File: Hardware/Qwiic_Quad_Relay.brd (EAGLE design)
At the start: 82.5 x 47 mm, 129 parts, among them J2 Qwiic Right Angle, J3 Qwiic Right Angle, J4 POWER_JACK, J9 AVR_SPI_PROG_3X2TESTPOINTS, K1 RELAY-SPDT-JZC-11F, K2 RELAY-SPDT-JZC-11F, K3 RELAY-SPDT-JZC-11F, K4 RELAY-SPDT-JZC-11F, Q1 600mA/40V, Q2 600mA/40V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

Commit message: Removes Buzzard lables and old production files
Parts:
- moved FRAME1 19.2 mm to (7.62, -12.7)
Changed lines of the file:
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@@
 <setting verticaltext="up"/>
 </settings>
-<grid distance="0.05" unitdist="inch" unit="inch" style="lines" multiple="1" display="yes" altdistance="0.002" altunitdist="inch" altunit="inch"/>
+<grid distance="0.05" unitdist="inch" unit="inch" style="lines" multiple="1" display="yes" altdistance="0.005" altunitdist="inch" altunit="inch"/>
 <layers>
 <layer number="1" name="Top" color="4" fill="1" visible="yes" active="yes"/>
@@
 <layer number="115" name="ReferenceISLANDS" color="7" fill="1" visible="no" active="no"/>
 <layer number="116" name="Patch_BOT" color="9" fill="4" visible="no" active="no"/>
-<layer number="117" name="PM_Ref" color="26" fill="1" visible="no" active="yes"/>
+<layer number="117" name="PM_Ref" color="26" fill="1" visible="yes" active="yes"/>
 <layer number="118" name="Rect_Pads" color="7" fill="1" visible="no" active="no"/>
-<layer number="119" name="PF_Ref" color="31" fill="1" visible="no" active="yes"/>
-<layer number="120" name="WFL_Ref" color="25" fill="1" visible="no" active="yes"/>
+<layer number="119" name="PF_Ref" color="31" fill="1" visible="yes" active="yes"/>
+<layer number="120" name="WFL_Ref" color="25" fill="1" visible="yes" active="yes"/>
 <layer number="121" name="_tsilk" color="7" fill="1" visible="no" active="no"/>
 <layer number="122" name="_bsilk" color="7" fill="1" visible="no" active="no"/>
@@
 <wire x1="82.55" y1="2.54" x2="82.55" y2="44.45" width="0.2032" layer="20"/>
 <wire x1="82.55" y1="44.45" x2="80.01" y2="46.99" width="0.2032" layer="20" curve="90"/>
-<text x="40.513" y="-16.637" size="1.778" layer="51" font="vector">Elias Santistevan</text>
+<text x="39.243" y="-12.827" size="1.778" layer="51" font="vector">Elias Santistevan</text>
 <text x="81.534" y="12.319" size="1.778" layer="16" font="vector" ratio="15" rot="SMR270">v20</text>
 <text x="24.892" y="19.812" size="0.381" layer="20" font="vector" rot="R90">Route Out</text>
@@
 <attribute name="VALUE" x="56.9722" y="37.7698" size="0.6096" layer="27" font="vector" ratio="20" align="bottom-center"/>
 </element>
-<element name="FRAME1" library="SparkFun-Aesthetics" package="CREATIVE_COMMONS" value="FRAME-LEDGER" x="10.16" y="-31.75" smashed="yes">
-<attribute name="DESIGNER" value="" x="10.16" y="-31.75" size="1.778" layer="27" display="off"/>
-<attribute name="REV" value="" x="10.16" y="-31.75" size="1.778" layer="27" display="off"/>
+<element name="FRAME1" library="SparkFun-Aesthetics" package="CREATIVE_COMMONS" value="FRAME-LEDGER" x="7.62" y="-12.7" smashed="yes">
+<attribute name="DESIGNER" value="" x="7.62" y="-12.7" size="1.778" layer="27" display="off"/>
+<attribute name="REV" value="" x="7.62" y="-12.7" size="1.778" layer="27" display="off"/>
 </element>
 <element name="C2" library="SparkFun-Capacitors" package="0402" value="0.1uF" x="54.8132" y="43.1546" smashed="yes" rot="R90">

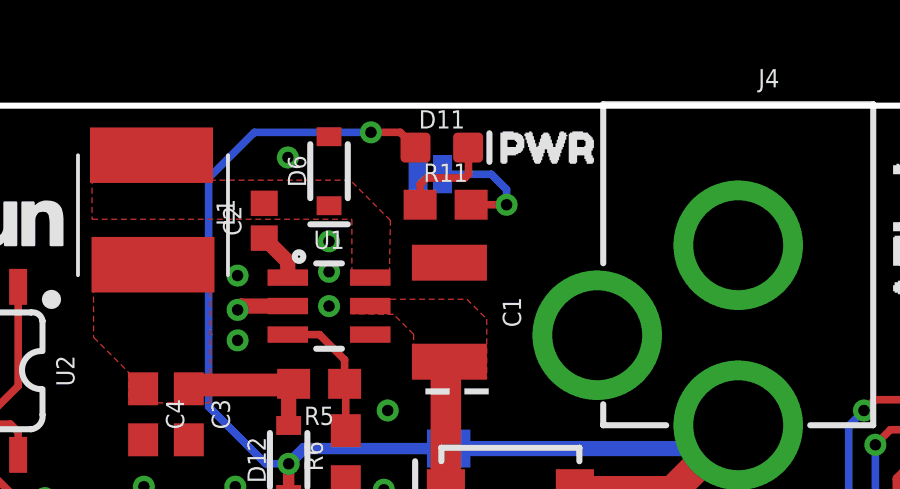
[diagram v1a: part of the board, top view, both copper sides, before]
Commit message: Changes LED jumper to normally closed with trace
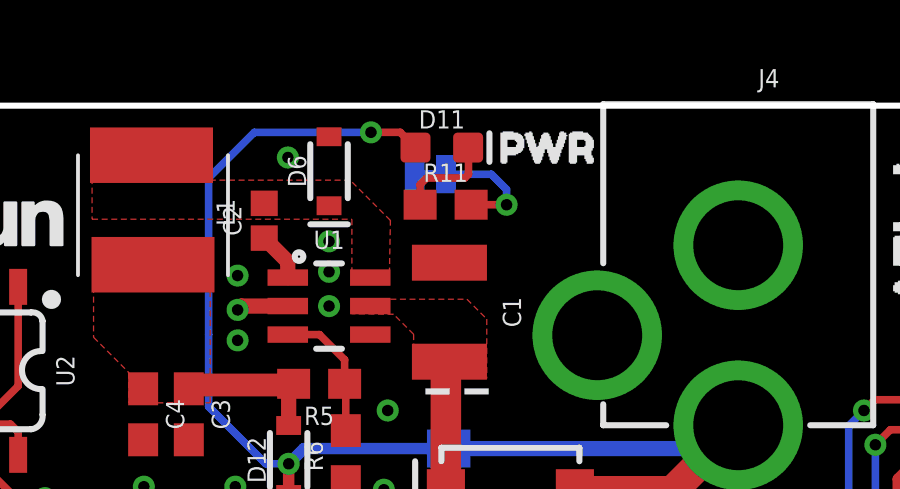
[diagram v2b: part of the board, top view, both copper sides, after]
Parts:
- LED: value JUMPER-SMT_2_NO_SILK -> JUMPER-SMT_2_NC_TRACE_SILK; device SparkFun-Jumpers:SMT-JUMPER_2_NO_SILK -> SparkFun-Jumpers:SMT-JUMPER_2_NC_TRACE_SILK
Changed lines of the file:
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@@
 <?xml version="1.0" encoding="utf-8"?>
 <!DOCTYPE eagle SYSTEM "eagle.dtd">
-<eagle version="9.5.2">
+<eagle version="9.5.1">
 <drawing>
 <settings>
@@
 <attribute name="VALUE" x="57.7342" y="44.8056" size="0.6096" layer="27" font="vector" ratio="20" rot="R90" align="top-center"/>
 </element>
-<element name="LED" library="SparkFun-Jumpers" package="SMT-JUMPER_2_NO_SILK" package3d_urn="urn:adsk.eagle:package:39279/1" value="JUMPER-SMT_2_NO_SILK" x="60.3504" y="44.704" smashed="yes" rot="MR180">
+<element name="LED" library="SparkFun-Jumpers" package="SMT-JUMPER_2_NC_TRACE_SILK" package3d_urn="urn:adsk.eagle:package:39281/1" value="JUMPER-SMT_2_NC_TRACE_SILK" x="60.3504" y="44.704" smashed="yes" rot="MR180">
 <attribute name="NAME" x="60.3504" y="43.561" size="0.6096" layer="26" font="vector" ratio="20" rot="MR180" align="bottom-center"/>
 <attribute name="VALUE" x="60.3504" y="45.847" size="0.6096" layer="28" font="vector" ratio="20" rot="MR180" align="top-center"/>
@@
 <wire x1="62.8904" y1="43.688" x2="62.8904" y2="44.196" width="0.254" layer="16"/>
 <wire x1="62.8904" y1="44.196" x2="62.3824" y2="44.704" width="0.254" layer="16"/>
-<wire x1="62.3824" y1="44.704" x2="60.7568" y2="44.704" width="0.254" layer="16"/>
+<wire x1="62.3824" y1="44.704" x2="60.8711" y2="44.704" width="0.254" layer="16"/>
 </signal>
 <signal name="N$1">

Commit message: Replaces 33 Ohm resistors with 0 Ohm
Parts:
- R10, R2, R4, R8: value 33 -> 0
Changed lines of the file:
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@@
 <attribute name="VALUE" x="20.447" y="19.05" size="0.6096" layer="27" font="vector" ratio="20" rot="R270" align="top-center"/>
 </element>
-<element name="R2" library="SparkFun-Resistors" package="0603" value="33" x="16.637" y="28.1266" smashed="yes" rot="R90">
+<element name="R2" library="SparkFun-Resistors" package="0603" value="0" x="16.637" y="28.1266" smashed="yes" rot="R90">
 <attribute name="NAME" x="15.875" y="28.1266" size="0.6096" layer="25" font="vector" ratio="20" rot="R90" align="bottom-center"/>
-<attribute name="PROD_ID" value="RES-08270" x="16.637" y="28.1266" size="1.778" layer="27" rot="R90" display="off"/>
-<attribute name="VALUE" value="33" x="17.399" y="28.1266" size="0.6096" layer="27" font="vector" ratio="20" rot="R90" align="top-center"/>
+<attribute name="PROD_ID" value="RES-08609" x="16.637" y="28.1266" size="1.778" layer="27" rot="R90" display="off"/>
+<attribute name="VALUE" value="0" x="17.399" y="28.1266" size="0.6096" layer="27" font="vector" ratio="20" rot="R90" align="top-center"/>
 </element>
 <element name="R1" library="SparkFun-Resistors" package="0603" value="1k" x="9.017" y="28.1266" smashed="yes" rot="R90">
@@
 <attribute name="VALUE" x="38.735" y="27.92105" size="0.6096" layer="27" font="vector" ratio="20" rot="R270" align="top-center"/>
 </element>
-<element name="R4" library="SparkFun-Resistors" package="0603" value="33" x="37.211" y="27.9996" smashed="yes" rot="R90">
+<element name="R4" library="SparkFun-Resistors" package="0603" value="0" x="37.211" y="27.9996" smashed="yes" rot="R90">
 <attribute name="NAME" x="36.449" y="27.9996" size="0.6096" layer="25" font="vector" ratio="20" rot="R90" align="bottom-center"/>
-<attribute name="PROD_ID" value="RES-08270" x="37.211" y="27.9996" size="1.778" layer="27" font="vector" ratio="15" rot="R90" display="off"/>
-<attribute name="VALUE" value="33" x="37.973" y="27.9996" size="0.6096" layer="27" font="vector" ratio="20" rot="R90" align="top-center"/>
+<attribute name="PROD_ID" value="RES-08609" x="37.211" y="27.9996" size="1.778" layer="27" font="vector" ratio="15" rot="R90" display="off"/>
+<attribute name="VALUE" value="0" x="37.973" y="27.9996" size="0.6096" layer="27" font="vector" ratio="20" rot="R90" align="top-center"/>
 </element>
-<element name="R8" library="SparkFun-Resistors" package="0603" value="33" x="57.404" y="27.9996" smashed="yes" rot="R90">
+<element name="R8" library="SparkFun-Resistors" package="0603" value="0" x="57.404" y="27.9996" smashed="yes" rot="R90">
 <attribute name="NAME" x="56.642" y="27.9996" size="0.6096" layer="25" font="vector" ratio="20" rot="R90" align="bottom-center"/>
-<attribute name="PROD_ID" value="RES-08270" x="57.404" y="27.9996" size="1.778" layer="27" font="vector" ratio="15" rot="R90" display="off"/>
-<attribute name="VALUE" value="33" x="58.166" y="27.9996" size="0.6096" layer="27" font="vector" ratio="20" rot="R90" align="top-center"/>
+<attribute name="PROD_ID" value="RES-08609" x="57.404" y="27.9996" size="1.778" layer="27" font="vector" ratio="15" rot="R90" display="off"/>
+<attribute name="VALUE" value="0" x="58.166" y="27.9996" size="0.6096" layer="27" font="vector" ratio="20" rot="R90" align="top-center"/>
 </element>
-<element name="R10" library="SparkFun-Resistors" package="0603" value="33" x="77.978" y="27.7837" smashed="yes" rot="R90">
+<element name="R10" library="SparkFun-Resistors" package="0603" value="0" x="77.978" y="27.7837" smashed="yes" rot="R90">
 <attribute name="NAME" x="77.216" y="27.7837" size="0.6096" layer="25" font="vector" ratio="20" rot="R90" align="bottom-center"/>
-<attribute name="PROD_ID" value="RES-08270" x="77.978" y="27.7837" size="1.778" layer="27" font="vector" ratio="15" rot="R90" display="off"/>
-<attribute name="VALUE" value="33" x="78.74" y="27.7837" size="0.6096" layer="27" font="vector" ratio="20" rot="R90" align="top-center"/>
+<attribute name="PROD_ID" value="RES-08609" x="77.978" y="27.7837" size="1.778" layer="27" font="vector" ratio="15" rot="R90" display="off"/>
+<attribute name="VALUE" value="0" x="78.74" y="27.7837" size="0.6096" layer="27" font="vector" ratio="20" rot="R90" align="top-center"/>
 </element>
 <element name="D4" library="SparkFun-LED" package="LED-0603" value="BLUE" x="32.258" y="28.15565" smashed="yes" rot="R270">

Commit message: Replaces clamping diode with something more suitable to stated maximum input voltage of the product.
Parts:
- D6: value 3A/10V/280mV -> 1A/23V/620mV
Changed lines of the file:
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@@
 <?xml version="1.0" encoding="utf-8"?>
 <!DOCTYPE eagle SYSTEM "eagle.dtd">
-<eagle version="9.5.1">
+<eagle version="9.6.2">
 <drawing>
 <settings>
@@
 <layer number="56" name="wert" color="7" fill="1" visible="no" active="no"/>
 <layer number="57" name="tCAD" color="7" fill="1" visible="no" active="no"/>
+<layer number="58" name="bCAD" color="7" fill="1" visible="no" active="no"/>
 <layer number="59" name="tCarbon" color="7" fill="1" visible="no" active="no"/>
 <layer number="60" name="bCarbon" color="7" fill="1" visible="no" active="no"/>
@@
 <layer number="128" name="_bValues" color="7" fill="1" visible="no" active="no"/>
 <layer number="129" name="Mask" color="7" fill="1" visible="no" active="no"/>
+<layer number="130" name="SMDSTROOK" color="7" fill="1" visible="no" active="no"/>
 <layer number="131" name="tAdjust" color="7" fill="1" visible="no" active="no"/>
 <layer number="132" name="bAdjust" color="7" fill="1" visible="no" active="no"/>
+<layer number="133" name="bottom_silk" color="7" fill="1" visible="no" active="no"/>
+<layer number="134" name="silk_top" color="7" fill="1" visible="no" active="no"/>
+<layer number="135" name="silk_bottom" color="7" fill="1" visible="no" active="no"/>
+<layer number="136" name="silktop" color="7" fill="1" visible="no" active="no"/>
+<layer number="137" name="silkbottom" color="7" fill="1" visible="no" active="no"/>
+<layer number="138" name="EEE" color="7" fill="1" visible="no" active="no"/>
+<layer number="139" name="_tKeepout" color="7" fill="1" visible="no" active="no"/>
+<layer number="140" name="mbKeepout" color="7" fill="1" visible="no" active="no"/>
+<layer number="141" name="ASSEMBLY_TOP" color="7" fill="1" visible="no" active="no"/>
+<layer number="142" name="mbRestrict" color="7" fill="1" visible="no" active="no"/>
+<layer number="143" name="PLACE_BOUND_TOP" color="7" fill="1" visible="no" active="no"/>
 <layer number="144" name="Drill_legend" color="7" fill="1" visible="no" active="no"/>
+<layer number="145" name="DrillLegend_01-16" color="7" fill="1" visible="no" active="no"/>
+<layer number="146" name="DrillLegend_01-20" color="7" fill="1" visible="no" active="no"/>
+<layer number="147" name="PIN_NUMBER" color="7" fill="1" visible="no" active="no"/>
+<layer number="148" name="DrillLegend_01-20" color="7" fill="1" visible="no" active="no"/>
+<layer number="149" name="DrillLegend_02-15" color="7" fill="1" visible="no" active="no"/>
 <layer number="150" name="Notes" color="7" fill="1" visible="no" active="no"/>
 <layer number="151" name="HeatSink" color="7" fill="1" visible="no" active="no"/>
@@
 <layer number="154" name="FabDoc2" color="7" fill="1" visible="no" active="no"/>
 <layer number="155" name="FabDoc3" color="7" fill="1" visible="no" active="no"/>
+<layer number="156" name="gesam-Maß" color="1" fill="7" visible="no" active="no"/>
+<layer number="157" name="FaceMchng" color="3" fill="1" visible="no" active="no"/>
+<layer number="158" name="FaceMMeas" color="3" fill="1" visible="no" active="no"/>
+<layer number="159" name="Geh-Bear2" color="1" fill="7" visible="no" active="no"/>
+<layer number="160" name="Topologie" color="9" fill="1" visible="no" active="no"/>
+<layer number="161" name="tomplace2" color="7" fill="1" visible="no" active="no"/>
+<layer number="166" name="AntennaArea" color="7" fill="1" visible="no" active="no"/>
+<layer number="168" name="4mmHeightArea" color="7" fill="1" visible="no" active="no"/>
+<layer number="191" name="mNets" color="7" fill="1" visible="no" active="no"/>
+<layer number="192" name="mBusses" color="7" fill="1" visible="no" active="no"/>
+<layer number="193" name="mPins" color="7" fill="1" visible="no" active="no"/>
+<layer number="194" name="mSymbols" color="7" fill="1" visible="no" active="no"/>
+<layer number="195" name="mNames" color="7" fill="1" visible="no" active="no"/>
+<layer number="196" name="mValues" color="7" fill="1" visible="no" active="no"/>
 <layer number="199" name="Contour" color="7" fill="1" visible="no" active="no"/>
 <layer number="200" name="200bmp" color="1" fill="10" visible="no" active="no"/>
@@
 <layer number="250" name="Descript" color="3" fill="1" visible="no" active="no"/>
 <layer number="251" name="SMDround" color="12" fill="11" visible="no" active="no"/>
+<layer number="252" name="BR-BS" color="7" fill="1" visible="no" active="no"/>
+<layer number="253" name="Extra" color="7" fill="1" visible="no" active="no"/>
 <layer number="254" name="cooling" color="7" fill="1" visible="no" active="no"/>
 <layer number="255" name="routoute" color="7" fill="1" visible="no" active="no"/>
@@
 <attribute name="VALUE" value="12k" x="56.642" y="38.481" size="0.6096" layer="27" font="vector" ratio="20" rot="R180" align="top-center"/>
 </element>
-<element name="D6" library="SparkFun-DiscreteSemi" package="SOD-323" value="3A/10V/280mV" x="56.9722" y="44.8056" smashed="yes" rot="R90">
+<element name="D6" library="SparkFun-DiscreteSemi" package="SOD-323" value="1A/23V/620mV" x="56.9722" y="44.8056" smashed="yes" rot="R90">
 <attribute name="NAME" x="56.2102" y="44.8056" size="0.6096" layer="25" font="vector" ratio="20" rot="R90" align="bottom-center"/>
-<attribute name="PROD_ID" value="DIO-14072" x="56.9722" y="44.8056" size="1.778" layer="27" rot="R90" display="off"/>
-<attribute name="VALUE" x="57.7342" y="44.8056" size="0.6096" layer="27" font="vector" ratio="20" rot="R90" align="top-center"/>
+<attribute name="PROD_ID" value="DIO-11623" x="56.9722" y="44.8056" size="1.778" layer="27" rot="R90" display="off"/>
+<attribute name="VALUE" value="1A/23V/620mV" x="57.7342" y="44.8056" size="0.6096" layer="27" font="vector" ratio="20" rot="R90" align="top-center"/>
 </element>
 <element name="LED" library="SparkFun-Jumpers" package="SMT-JUMPER_2_NC_TRACE_SILK" package3d_urn="urn:adsk.eagle:package:39281/1" value="JUMPER-SMT_2_NC_TRACE_SILK" x="60.3504" y="44.704" smashed="yes" rot="MR180">
